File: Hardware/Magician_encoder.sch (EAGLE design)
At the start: 33 parts, among them Q1 MMBT2222A, Q2 MMBT2222A, U1 QRE1113, U2 QRE1113

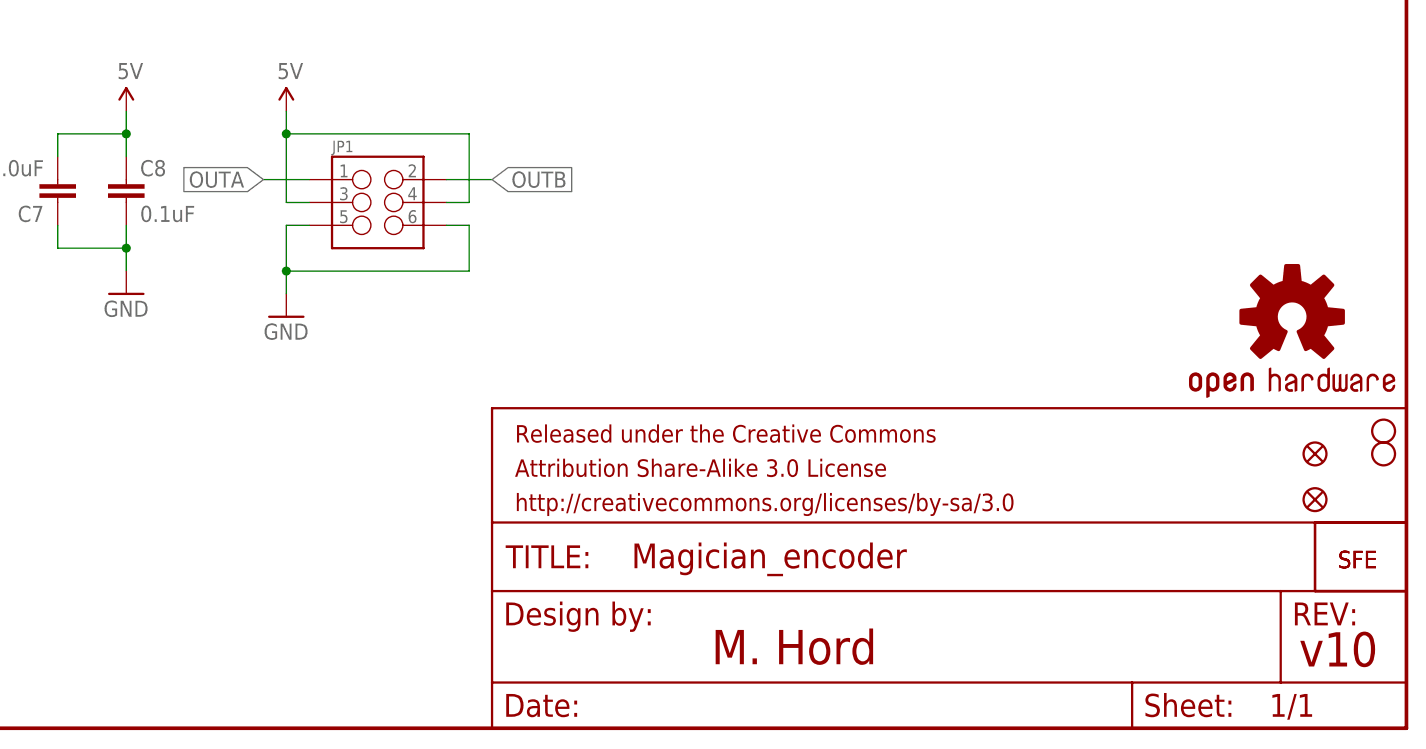
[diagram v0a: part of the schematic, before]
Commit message: Put male SMT header on back
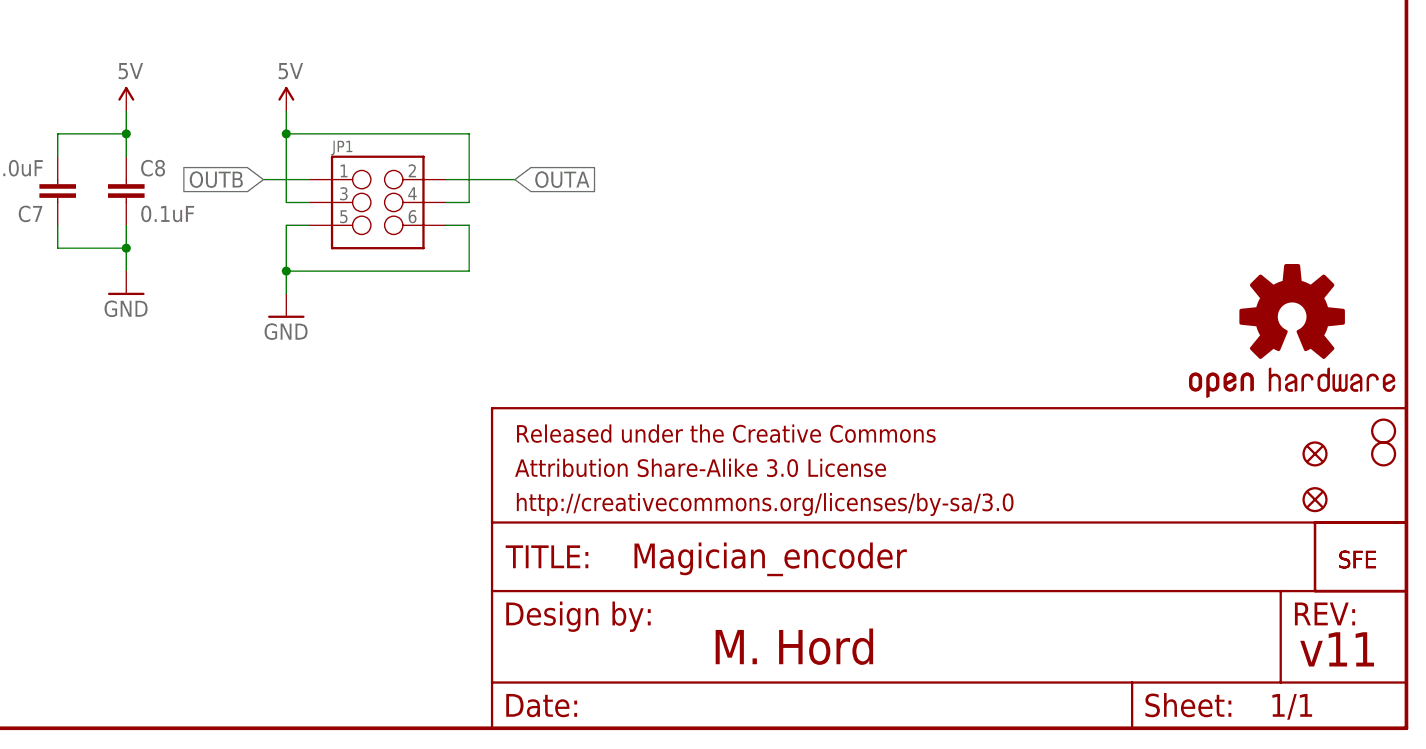
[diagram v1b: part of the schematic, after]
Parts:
- JP1: device SparkFun-Connectors:M03X22X3_SILK_SM -> SparkFun-Connectors:M03X2SMT
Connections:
- net OUTA: now also JP1.2; no longer JP1.1
- net OUTB: now also JP1.1; no longer JP1.2
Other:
- note added: "v11"
- note removed: "v10"
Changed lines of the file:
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@@
 <?xml version="1.0" encoding="utf-8"?>
 <!DOCTYPE eagle SYSTEM "eagle.dtd">
-<eagle version="6.5.0">
+<eagle version="6.4">
 <drawing>
 <settings>
@@
 <grid distance="0.1" unitdist="inch" unit="inch" style="lines" multiple="1" display="no" altdistance="0.01" altunitdist="inch" altunit="inch"/>
 <layers>
-<layer number="1" name="Top" color="4" fill="1" visible="no" active="no"/>
-<layer number="2" name="Route2" color="1" fill="3" visible="no" active="no"/>
-<layer number="3" name="Route3" color="4" fill="3" visible="no" active="no"/>
-<layer number="4" name="Route4" color="1" fill="4" visible="no" active="no"/>
-<layer number="5" name="Route5" color="4" fill="4" visible="no" active="no"/>
-<layer number="6" name="Route6" color="1" fill="8" visible="no" active="no"/>
-<layer number="7" name="Route7" color="4" fill="8" visible="no" active="no"/>
-<layer number="8" name="Route8" color="1" fill="2" visible="no" active="no"/>
-<layer number="9" name="Route9" color="4" fill="2" visible="no" active="no"/>
-<layer number="10" name="Route10" color="1" fill="7" visible="no" active="no"/>
-<layer number="11" name="Route11" color="4" fill="7" visible="no" active="no"/>
-<layer number="12" name="Route12" color="1" fill="5" visible="no" active="no"/>
-<layer number="13" name="Route13" color="4" fill="5" visible="no" active="no"/>
-<layer number="14" name="Route14" color="1" fill="6" visible="no" active="no"/>
-<layer number="15" name="Route15" color="4" fill="6" visible="no" active="no"/>
-<layer number="16" name="Bottom" color="1" fill="1" visible="no" active="no"/>
-<layer number="17" name="Pads" color="2" fill="1" visible="no" active="no"/>
-<layer number="18" name="Vias" color="2" fill="1" visible="no" active="no"/>
-<layer number="19" name="Unrouted" color="6" fill="1" visible="no" active="no"/>
-<layer number="20" name="Dimension" color="15" fill="1" visible="no" active="no"/>
-<layer number="21" name="tPlace" color="7" fill="1" visible="no" active="no"/>
-<layer number="22" name="bPlace" color="7" fill="1" visible="no" active="no"/>
-<layer number="23" name="tOrigins" color="15" fill="1" visible="no" active="no"/>
-<layer number="24" name="bOrigins" color="15" fill="1" visible="no" active="no"/>
-<layer number="25" name="tNames" color="7" fill="1" visible="no" active="no"/>
-<layer number="26" name="bNames" color="7" fill="1" visible="no" active="no"/>
-<layer number="27" name="tValues" color="7" fill="1" visible="no" active="no"/>
-<layer number="28" name="bValues" color="7" fill="1" visible="no" active="no"/>
+<layer number="1" name="Top" color="4" fill="1" visible="yes" active="no"/>
+<layer number="2" name="Route2" color="1" fill="3" visible="yes" active="no"/>
+<layer number="3" name="Route3" color="4" fill="3" visible="yes" active="no"/>
+<layer number="4" name="Route4" color="1" fill="4" visible="yes" active="no"/>
+<layer number="5" name="Route5" color="4" fill="4" visible="yes" active="no"/>
+<layer number="6" name="Route6" color="1" fill="8" visible="yes" active="no"/>
+<layer number="7" name="Route7" color="4" fill="8" visible="yes" active="no"/>
+<layer number="8" name="Route8" color="1" fill="2" visible="yes" active="no"/>
+<layer number="9" name="Route9" color="4" fill="2" visible="yes" active="no"/>
+<layer number="10" name="Route10" color="1" fill="7" visible="yes" active="no"/>
+<layer number="11" name="Route11" color="4" fill="7" visible="yes" active="no"/>
+<layer number="12" name="Route12" color="1" fill="5" visible="yes" active="no"/>
+<layer number="13" name="Route13" color="4" fill="5" visible="yes" active="no"/>
+<layer number="14" name="Route14" color="1" fill="6" visible="yes" active="no"/>
+<layer number="15" name="Route15" color="4" fill="6" visible="yes" active="no"/>
+<layer number="16" name="Bottom" color="1" fill="1" visible="yes" active="no"/>
+<layer number="17" name="Pads" color="2" fill="1" visible="yes" active="no"/>
+<layer number="18" name="Vias" color="2" fill="1" visible="yes" active="no"/>
+<layer number="19" name="Unrouted" color="6" fill="1" visible="yes" active="no"/>
+<layer number="20" name="Dimension" color="6" fill="1" visible="yes" active="no"/>
+<layer number="21" name="tPlace" color="16" fill="1" visible="yes" active="no"/>
+<layer number="22" name="bPlace" color="14" fill="1" visible="yes" active="no"/>
+<layer number="23" name="tOrigins" color="15" fill="1" visible="yes" active="no"/>
+<layer number="24" name="bOrigins" color="15" fill="1" visible="yes" active="no"/>
+<layer number="25" name="tNames" color="7" fill="1" visible="yes" active="no"/>
+<layer number="26" name="bNames" color="7" fill="1" visible="yes" active="no"/>
+<layer number="27" name="tValues" color="7" fill="1" visible="yes" active="no"/>
+<layer number="28" name="bValues" color="7" fill="1" visible="yes" active="no"/>
 <layer number="29" name="tStop" color="7" fill="3" visible="no" active="no"/>
 <layer number="30" name="bStop" color="7" fill="6" visible="no" active="no"/>
@@
 <layer number="35" name="tGlue" color="7" fill="4" visible="no" active="no"/>
 <layer number="36" name="bGlue" color="7" fill="5" visible="no" active="no"/>
-<layer number="37" name="tTest" color="7" fill="1" visible="no" active="no"/>
-<layer number="38" name="bTest" color="7" fill="1" visible="no" active="no"/>
+<layer number="37" name="tTest" color="7" fill="1" visible="yes" active="no"/>
+<layer number="38" name="bTest" color="7" fill="1" visible="yes" active="no"/>
 <layer number="39" name="tKeepout" color="4" fill="11" visible="no" active="no"/>
 <layer number="40" name="bKeepout" color="1" fill="11" visible="no" active="no"/>
@@
 <layer number="44" name="Drills" color="7" fill="1" visible="no" active="no"/>
 <layer number="45" name="Holes" color="7" fill="1" visible="no" active="no"/>
-<layer number="46" name="Milling" color="3" fill="1" visible="no" active="no"/>
-<layer number="47" name="Measures" color="7" fill="1" visible="no" active="no"/>
-<layer number="48" name="Document" color="7" fill="1" visible="no" active="no"/>
-<layer number="49" name="Reference" color="7" fill="1" visible="no" active="no"/>
-<layer number="50" name="dxf" color="7" fill="1" visible="no" active="no"/>
-<layer number="51" name="tDocu" color="7" fill="1" visible="no" active="no"/>
-<layer number="52" name="bDocu" color="7" fill="1" visible="no" active="no"/>
-<layer number="53" name="tGND_GNDA" color="7" fill="9" visible="no" active="no"/>
-<layer number="54" name="bGND_GNDA" color="1" fill="9" visible="no" active="no"/>
-<layer number="56" name="wert" color="7" fill="1" visible="no" active="no"/>
+<layer number="46" name="Milling" color="3" fill="1" visible="yes" active="no"/>
+<layer number="47" name="Measures" color="7" fill="1" visible="yes" active="no"/>
+<layer number="48" name="Document" color="7" fill="1" visible="yes" active="no"/>
+<layer number="49" name="Reference" color="7" fill="1" visible="yes" active="no"/>
+<layer number="50" name="dxf" color="7" fill="1" visible="yes" active="no"/>
+<layer number="51" name="tDocu" color="6" fill="1" visible="yes" active="no"/>
+<layer number="52" name="bDocu" color="7" fill="1" visible="yes" active="no"/>
+<layer number="53" name="tGND_GNDA" color="7" fill="9" visible="yes" active="no"/>
+<layer number="54" name="bGND_GNDA" color="1" fill="9" visible="yes" active="no"/>
+<layer number="56" name="wert" color="7" fill="1" visible="yes" active="no"/>
 <layer number="91" name="Nets" color="2" fill="1" visible="yes" active="yes"/>
 <layer number="92" name="Busses" color="1" fill="1" visible="yes" active="yes"/>
@@
 <part name="C8" library="SparkFun-Capacitors" deviceset="0.1UF-25V(+80/-20%)(0603)" device="" value="0.1uF"/>
 <part name="U1" library="SparkFun-Sensors" deviceset="QRE1113" device=""/>
-<part name="JP1" library="SparkFun-Connectors" deviceset="M03X2" device="2X3_SILK_SM"/>
+<part name="JP1" library="SparkFun-Connectors" deviceset="M03X2" device="SMT"/>
 <part name="R1" library="SparkFun-Resistors" deviceset="100OHM1/10W1%(0603)" device="" value="100"/>
 <part name="SUPPLY3" library="SparkFun-Aesthetics" deviceset="5V" device=""/>
@@
 <sheet>
 <plain>
-<text x="236.982" y="6.858" size="3.81" layer="94">v10</text>
+<text x="236.982" y="6.858" size="3.81" layer="94">v11</text>
 <text x="171.704" y="7.112" size="3.81" layer="94">M. Hord</text>
 </plain>
@@
 <net name="OUTA" class="0">
 <segment>
-<pinref part="JP1" gate="G$1" pin="1"/>
-<wire x1="127" y1="60.96" x2="121.92" y2="60.96" width="0.1524" layer="91"/>
-<label x="121.92" y="60.96" size="1.778" layer="95" rot="R180" xref="yes"/>
-</segment>
-<segment>
 <pinref part="R5" gate="G$1" pin="1"/>
 <wire x1="93.98" y1="142.24" x2="93.98" y2="137.16" width="0.1524" layer="91"/>
@@
 <pinref part="Q1" gate="G$1" pin="C"/>
 </segment>
+<segment>
+<pinref part="JP1" gate="G$1" pin="2"/>
+<wire x1="142.24" y1="60.96" x2="149.86" y2="60.96" width="0.1524" layer="91"/>
+<label x="149.86" y="60.96" size="1.778" layer="95" xref="yes"/>
+</segment>
 </net>
 <net name="N$5" class="0">
@@
 </net>
 <net name="OUTB" class="0">
-<segment>
-<pinref part="JP1" gate="G$1" pin="2"/>
-<wire x1="142.24" y1="60.96" x2="147.32" y2="60.96" width="0.1524" layer="91"/>
-<label x="147.32" y="60.96" size="1.778" layer="95" xref="yes"/>
-</segment>
 <segment>
 <pinref part="R11" gate="G$1" pin="1"/>
@@
 <pinref part="Q2" gate="G$1" pin="C"/>
 </segment>
+<segment>
+<pinref part="JP1" gate="G$1" pin="1"/>
+<wire x1="127" y1="60.96" x2="121.92" y2="60.96" width="0.1524" layer="91"/>
+<label x="121.92" y="60.96" size="1.778" layer="95" rot="R180" xref="yes"/>
+</segment>
 </net>
